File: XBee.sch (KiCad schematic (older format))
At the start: 3 parts, among them U2 XBEE

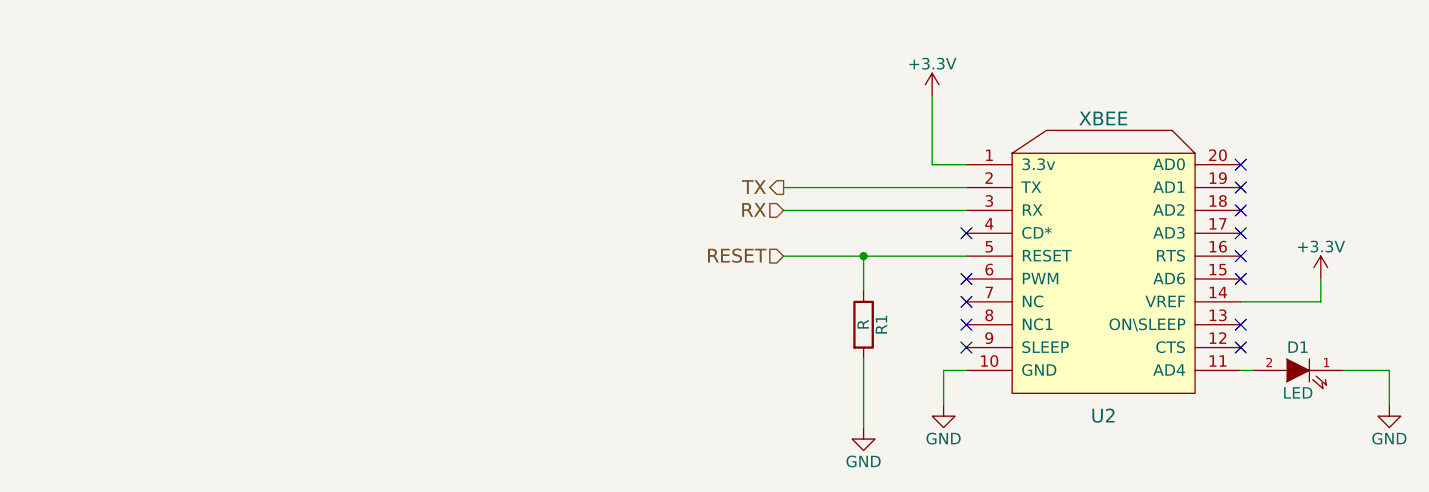
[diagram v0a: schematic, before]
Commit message: Placement in progress. XBee module 3d model
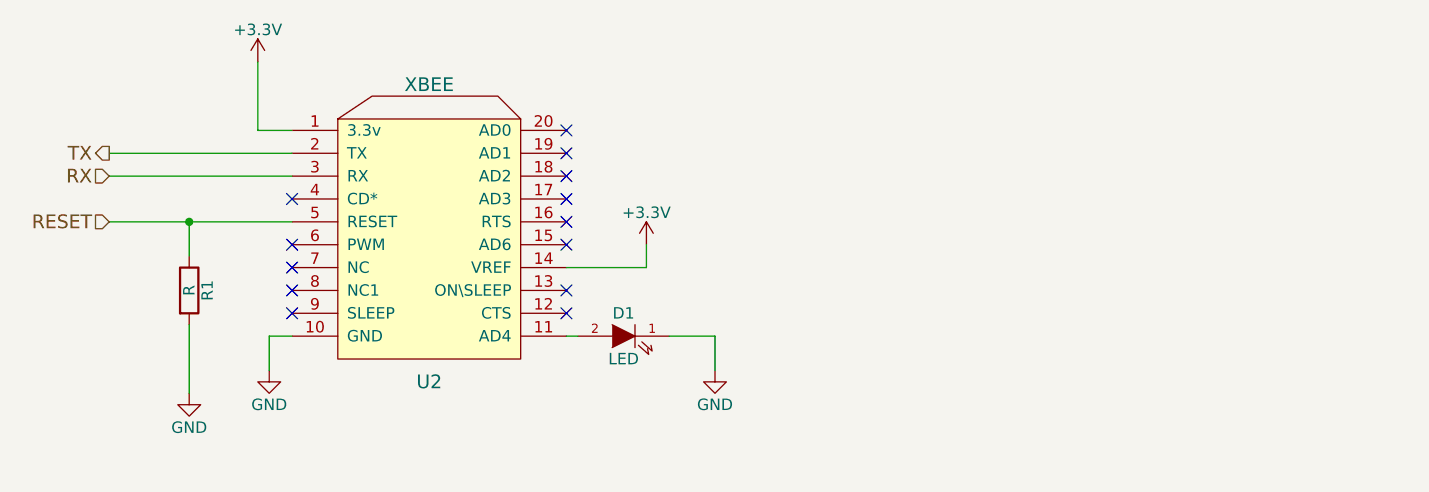
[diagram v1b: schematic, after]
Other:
- moved on the sheet: D1, R1, U2
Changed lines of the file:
@@
 Comment4 ""
 $EndDescr
-Text HLabel 5450 3200 0    60   Input ~ 0
+Text HLabel 2500 3050 0    60   Input ~ 0
 RESET
-Text HLabel 5450 2900 0    60   Output ~ 0
+Text HLabel 2500 2750 0    60   Output ~ 0
 TX
-Text HLabel 5450 3000 0    60   Input ~ 0
+Text HLabel 2500 2850 0    60   Input ~ 0
 RX
 Wire Wire Line
-	5450 2900 6250 2900
+	2500 2750 3300 2750
 Wire Wire Line
-	5450 3000 6250 3000
+	2500 2850 3300 2850
 Wire Wire Line
-	5450 3200 6250 3200
+	2500 3050 3300 3050
 $Comp
 L R R1
 U 1 1 583259C8
-P 5800 3500
-F 0 "R1" V 5880 3500 50  0000 C CNN
-F 1 "R" V 5800 3500 50  0000 C CNN
-F 2 "footprints:R_0603" V 5730 3500 50  0001 C CNN
-F 3 "" H 5800 3500 50  0000 C CNN
-	1    5800 3500
+P 2850 3350
+F 0 "R1" V 2930 3350 50  0000 C CNN
+F 1 "R" V 2850 3350 50  0000 C CNN
+F 2 "footprints:R_0603" V 2780 3350 50  0001 C CNN
+F 3 "" H 2850 3350 50  0000 C CNN
+	1    2850 3350
 	1    0    0    -1
 $EndComp
@@
 L LED D1
 U 1 1 583259E1
-P 7700 3700
-F 0 "D1" H 7700 3800 50  0000 C CNN
-F 1 "LED" H 7700 3600 50  0000 C CNN
-F 2 "footprints:LED-3MM" H 7700 3700 50  0001 C CNN
-F 3 "" H 7700 3700 50  0000 C CNN
-	1    7700 3700
+P 4750 3550
+F 0 "D1" H 4750 3650 50  0000 C CNN
+F 1 "LED" H 4750 3450 50  0000 C CNN
+F 2 "footprints:LED-3MM" H 4750 3550 50  0001 C CNN
+F 3 "" H 4750 3550 50  0000 C CNN
+	1    4750 3550
 	-1   0    0    -1
 $EndComp
@@
 L GND #PWR011
 U 1 1 583259FC
-P 8100 3850
-F 0 "#PWR011" H 8100 3600 50  0001 C CNN
-F 1 "GND" H 8100 3700 50  0000 C CNN
-F 2 "" H 8100 3850 50  0000 C CNN
-F 3 "" H 8100 3850 50  0000 C CNN
-	1    8100 3850
+P 5150 3700
+F 0 "#PWR011" H 5150 3450 50  0001 C CNN
+F 1 "GND" H 5150 3550 50  0000 C CNN
+F 2 "" H 5150 3700 50  0000 C CNN
+F 3 "" H 5150 3700 50  0000 C CNN
+	1    5150 3700
 	1    0    0    -1
 $EndComp
@@
 L GND #PWR012
 U 1 1 58325A17
-P 6150 3850
-F 0 "#PWR012" H 6150 3600 50  0001 C CNN
-F 1 "GND" H 6150 3700 50  0000 C CNN
-F 2 "" H 6150 3850 50  0000 C CNN
-F 3 "" H 6150 3850 50  0000 C CNN
-	1    6150 3850
+P 3200 3700
+F 0 "#PWR012" H 3200 3450 50  0001 C CNN
+F 1 "GND" H 3200 3550 50  0000 C CNN
+F 2 "" H 3200 3700 50  0000 C CNN
+F 3 "" H 3200 3700 50  0000 C CNN
+	1    3200 3700
 	1    0    0    -1
 $EndComp
@@
 L GND #PWR013
 U 1 1 58325A2B
-P 5800 3950
-F 0 "#PWR013" H 5800 3700 50  0001 C CNN
-F 1 "GND" H 5800 3800 50  0000 C CNN
-F 2 "" H 5800 3950 50  0000 C CNN
-F 3 "" H 5800 3950 50  0000 C CNN
-	1    5800 3950
+P 2850 3800
+F 0 "#PWR013" H 2850 3550 50  0001 C CNN
+F 1 "GND" H 2850 3650 50  0000 C CNN
+F 2 "" H 2850 3800 50  0000 C CNN
+F 3 "" H 2850 3800 50  0000 C CNN
+	1    2850 3800
 	1    0    0    -1
 $EndComp
@@
 L +3.3V #PWR014
 U 1 1 58325A3E
-P 6100 2500
-F 0 "#PWR014" H 6100 2350 50  0001 C CNN
-F 1 "+3.3V" H 6100 2640 50  0000 C CNN
-F 2 "" H 6100 2500 50  0000 C CNN
-F 3 "" H 6100 2500 50  0000 C CNN
-	1    6100 2500
+P 3150 2350
+F 0 "#PWR014" H 3150 2200 50  0001 C CNN
+F 1 "+3.3V" H 3150 2490 50  0000 C CNN
+F 2 "" H 3150 2350 50  0000 C CNN
+F 3 "" H 3150 2350 50  0000 C CNN
+	1    3150 2350
 	1    0    0    -1
 $EndComp
 Wire Wire Line
-	6100 2500 6100 2800
+	3150 2350 3150 2650
 Wire Wire Line
-	6100 2800 6250 2800
+	3150 2650 3300 2650
 Wire Wire Line
-	5800 3350 5800 3200
-Connection ~ 5800 3200
+	2850 3200 2850 3050
+Connection ~ 2850 3050
 Wire Wire Line
-	6250 3700 6150 3700
+	3300 3550 3200 3550
 Wire Wire Line
-	6150 3700 6150 3850
-NoConn ~ 6250 3100
-NoConn ~ 6250 3300
-NoConn ~ 6250 3400
-NoConn ~ 6250 3500
-NoConn ~ 6250 3600
-NoConn ~ 7450 3500
-NoConn ~ 7450 3600
-NoConn ~ 7450 2800
-NoConn ~ 7450 2900
-NoConn ~ 7450 3000
-NoConn ~ 7450 3100
-NoConn ~ 7450 3200
-NoConn ~ 7450 3300
+	3200 3550 3200 3700
+NoConn ~ 3300 2950
+NoConn ~ 3300 3150
+NoConn ~ 3300 3250
+NoConn ~ 3300 3350
+NoConn ~ 3300 3450
+NoConn ~ 4500 3350
+NoConn ~ 4500 3450
+NoConn ~ 4500 2650
+NoConn ~ 4500 2750
+NoConn ~ 4500 2850
+NoConn ~ 4500 2950
+NoConn ~ 4500 3050
+NoConn ~ 4500 3150
 $Comp
 L +3.3V #PWR015
 U 1 1 58325B5C
-P 7800 3300
-F 0 "#PWR015" H 7800 3150 50  0001 C CNN
-F 1 "+3.3V" H 7800 3440 50  0000 C CNN
-F 2 "" H 7800 3300 50  0000 C CNN
-F 3 "" H 7800 3300 50  0000 C CNN
-	1    7800 3300
+P 4850 3150
+F 0 "#PWR015" H 4850 3000 50  0001 C CNN
+F 1 "+3.3V" H 4850 3290 50  0000 C CNN
+F 2 "" H 4850 3150 50  0000 C CNN
+F 3 "" H 4850 3150 50  0000 C CNN
+	1    4850 3150
 	1    0    0    -1
 $EndComp
 Wire Wire Line
-	7800 3300 7800 3400
+	4850 3150 4850 3250
 Wire Wire Line
-	7800 3400 7450 3400
+	4850 3250 4500 3250
 Wire Wire Line
-	7500 3700 7450 3700
+	4550 3550 4500 3550
 Wire Wire Line
-	7900 3700 8100 3700
+	4950 3550 5150 3550
 Wire Wire Line
-	8100 3700 8100 3850
+	5150 3550 5150 3700
 Wire Wire Line
-	5800 3650 5800 3950
+	2850 3500 2850 3800
 $Comp
 L XBEE U2
 U 1 1 58325202
-P 6850 3350
-F 0 "U2" H 6850 2800 60  0000 C CNN
-F 1 "XBEE" H 6850 4100 60  0000 C CNN
-F 2 "XBee:XBee-pro" H 6850 3350 60  0001 C CNN
-F 3 "" H 6850 3350 60  0000 C CNN
-	1    6850 3350
+P 3900 3200
+F 0 "U2" H 3900 2650 60  0000 C CNN
+F 1 "XBEE" H 3900 3950 60  0000 C CNN
+F 2 "XBee:XBee-pro" H 3900 3200 60  0001 C CNN
+F 3 "" H 3900 3200 60  0000 C CNN
+	1    3900 3200
 	1    0    0    -1
 $EndComp

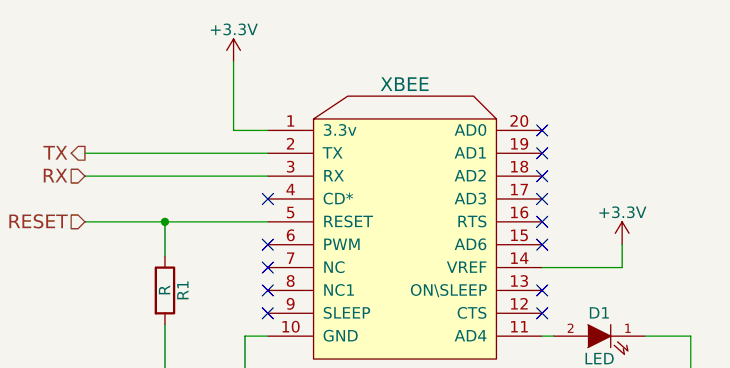
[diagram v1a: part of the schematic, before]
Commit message: Corregido: footprint batería, footprint GY-521, conector poncho para pasar ERC en esquemático, placement de footprints, dimensión del poncho para dejar descubierto el botón de reset de la EDU-CIAA. Agregado: agujeros de sujeción en la parte superior del poncho.
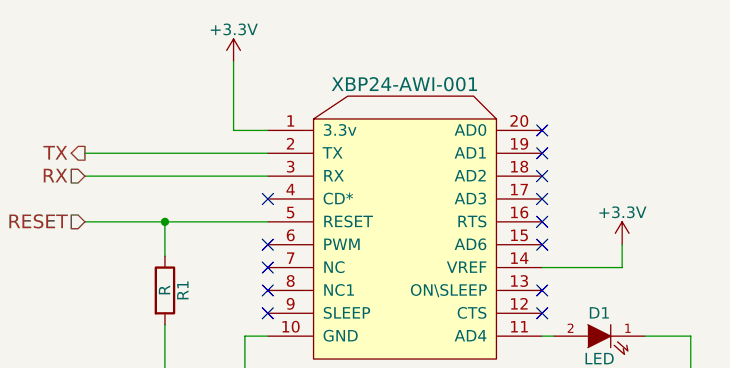
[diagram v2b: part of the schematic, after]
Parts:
- U2: value XBEE -> XBP24-AWI-001; Manf (none) -> DIGI
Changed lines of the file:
@@
 $EndComp
 $Comp
-L GND #PWR011
+L GND #PWR013
 U 1 1 583259FC
 P 5150 3700
-F 0 "#PWR011" H 5150 3450 50  0001 C CNN
+F 0 "#PWR013" H 5150 3450 50  0001 C CNN
 F 1 "GND" H 5150 3550 50  0000 C CNN
 F 2 "" H 5150 3700 50  0000 C CNN
@@
 $EndComp
 $Comp
-L GND #PWR012
+L GND #PWR014
 U 1 1 58325A17
 P 3200 3700
-F 0 "#PWR012" H 3200 3450 50  0001 C CNN
+F 0 "#PWR014" H 3200 3450 50  0001 C CNN
 F 1 "GND" H 3200 3550 50  0000 C CNN
 F 2 "" H 3200 3700 50  0000 C CNN
@@
 $EndComp
 $Comp
-L GND #PWR013
+L GND #PWR015
 U 1 1 58325A2B
 P 2850 3800
-F 0 "#PWR013" H 2850 3550 50  0001 C CNN
+F 0 "#PWR015" H 2850 3550 50  0001 C CNN
 F 1 "GND" H 2850 3650 50  0000 C CNN
 F 2 "" H 2850 3800 50  0000 C CNN
@@
 $EndComp
 $Comp
-L +3.3V #PWR014
+L +3.3V #PWR016
 U 1 1 58325A3E
 P 3150 2350
-F 0 "#PWR014" H 3150 2200 50  0001 C CNN
+F 0 "#PWR016" H 3150 2200 50  0001 C CNN
 F 1 "+3.3V" H 3150 2490 50  0000 C CNN
 F 2 "" H 3150 2350 50  0000 C CNN
@@
 NoConn ~ 4500 3150
 $Comp
-L +3.3V #PWR015
+L +3.3V #PWR017
 U 1 1 58325B5C
 P 4850 3150
-F 0 "#PWR015" H 4850 3000 50  0001 C CNN
+F 0 "#PWR017" H 4850 3000 50  0001 C CNN
 F 1 "+3.3V" H 4850 3290 50  0000 C CNN
 F 2 "" H 4850 3150 50  0000 C CNN
@@
 P 3900 3200
 F 0 "U2" H 3900 2650 60  0000 C CNN
-F 1 "XBEE" H 3900 3950 60  0000 C CNN
+F 1 "XBP24-AWI-001" H 3900 3950 60  0000 C CNN
 F 2 "XBee:XBee-pro" H 3900 3200 60  0001 C CNN
-F 3 "" H 3900 3200 60  0000 C CNN
+F 3 "https://www.digi.com/pdf/ds_xbeemultipointmodules.pdf" H 3900 3200 60  0001 C CNN
+F 4 "DIGI" H 3900 3200 60  0001 C CNN "Manf"
+F 5 "XB24-AWI-001
+" H 3900 3200 60  0001 C CNN "Manf#"
+F 6 "XB24-AWI-001-ND
+" H 3900 3200 60  0001 C CNN "Digikey#"
+F 7 "888-XB24-AWI-001
+" H 3900 3200 60  0001 C CNN "Mouser#"
 	1    3900 3200
 	1    0    0    -1

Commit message: Ruteo. Correciones. Cambio de footprint del switch.
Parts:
- U2: value XBP24-AWI-001 -> XBEE; footprint XBee:XBee-pro -> footprints:XBee-pro; Desc (none) -> XBee-PRO S1 802.15.4 extended-range module w/ wire antenna; Manf# (none) -> XBP24-AWI-001
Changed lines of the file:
@@
 encoding utf-8
 Sheet 3 4
-Title ""
-Date ""
-Rev ""
+Title "Poncho Misión SAEv2 - Módulo XBee"
+Date "2016-12-14"
+Rev "1.0"
 Comp ""
-Comment1 ""
-Comment2 ""
+Comment1 "Autores: Julián Iglesias / Elli Carlos"
+Comment2 "Licencia: BSD"
 Comment3 ""
 Comment4 ""
@@
 $Comp
 L XBEE U2
-U 1 1 58325202
+U 1 1 5851DFE8
 P 3900 3200
 F 0 "U2" H 3900 2650 60  0000 C CNN
-F 1 "XBP24-AWI-001" H 3900 3950 60  0000 C CNN
-F 2 "XBee:XBee-pro" H 3900 3200 60  0001 C CNN
+F 1 "XBEE" H 3900 3950 60  0000 C CNN
+F 2 "footprints:XBee-pro" H 3900 3200 60  0001 C CNN
 F 3 "https://www.digi.com/pdf/ds_xbeemultipointmodules.pdf" H 3900 3200 60  0001 C CNN
-F 4 "DIGI" H 3900 3200 60  0001 C CNN "Manf"
-F 5 "XB24-AWI-001
-" H 3900 3200 60  0001 C CNN "Manf#"
-F 6 "XB24-AWI-001-ND
+F 4 "XBee-PRO S1 802.15.4 extended-range module w/ wire antenna" H 3900 3200 60  0001 C CNN "Desc"
+F 5 "DIGI" H 3900 3200 60  0001 C CNN "Manf"
+F 6 "XBP24-AWI-001" H 3900 3200 60  0001 C CNN "Manf#"
+F 7 "XBP24-AWI-001-ND
 " H 3900 3200 60  0001 C CNN "Digikey#"
-F 7 "888-XB24-AWI-001
+F 8 "888-XBP24-AWI-001
 " H 3900 3200 60  0001 C CNN "Mouser#"
 	1    3900 3200

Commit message: Corrección de errores in progress...
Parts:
- U2: Desc XBee-PRO S1 802.15.4 extended-range module w/ wire antenna -> XBee Pro Series1 Wire antenna; Digikey# (none) -> XBP24-AWI-001-ND; Mouser# (none) -> 888-XBP24-AWI-001
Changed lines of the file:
@@
 EESchema Schematic File Version 2
-LIBS:Mision_SAE-rescue
 LIBS:power
-LIBS:device
-LIBS:conn
-LIBS:mpu-6050
-LIBS:power1
-LIBS:xbee
-LIBS:basico
-LIBS:GY-65
-LIBS:GY-521
 LIBS:Mision_SAE-cache
 EELAYER 25 0
@@
 encoding utf-8
 Sheet 3 4
-Title "Poncho Misión SAEv2 - Módulo XBee"
-Date "2016-12-14"
+Title "Poncho Misión SAEv2 - Esquemático jerárquico"
+Date "2016-12-21"
 Rev "1.0"
 Comp ""
-Comment1 "Autores: Julián Iglesias / Elli Carlos"
-Comment2 "Licencia: BSD"
-Comment3 ""
+Comment1 "Autores: Julián Iglesias / Elli Carlos."
+Comment2 "Revisor: Matías Marando"
+Comment3 "Licencia: BSD"
 Comment4 ""
 $EndDescr
@@
 $EndComp
 $Comp
-L GND #PWR013
+L GND #PWR011
 U 1 1 583259FC
 P 5150 3700
-F 0 "#PWR013" H 5150 3450 50  0001 C CNN
+F 0 "#PWR011" H 5150 3450 50  0001 C CNN
 F 1 "GND" H 5150 3550 50  0000 C CNN
 F 2 "" H 5150 3700 50  0000 C CNN
@@
 $EndComp
 $Comp
-L GND #PWR014
+L GND #PWR012
 U 1 1 58325A17
 P 3200 3700
-F 0 "#PWR014" H 3200 3450 50  0001 C CNN
+F 0 "#PWR012" H 3200 3450 50  0001 C CNN
 F 1 "GND" H 3200 3550 50  0000 C CNN
 F 2 "" H 3200 3700 50  0000 C CNN
@@
 $EndComp
 $Comp
-L GND #PWR015
+L GND #PWR013
 U 1 1 58325A2B
 P 2850 3800
-F 0 "#PWR015" H 2850 3550 50  0001 C CNN
+F 0 "#PWR013" H 2850 3550 50  0001 C CNN
 F 1 "GND" H 2850 3650 50  0000 C CNN
 F 2 "" H 2850 3800 50  0000 C CNN
@@
 $EndComp
 $Comp
-L +3.3V #PWR016
+L +3.3V #PWR014
 U 1 1 58325A3E
 P 3150 2350
-F 0 "#PWR016" H 3150 2200 50  0001 C CNN
+F 0 "#PWR014" H 3150 2200 50  0001 C CNN
 F 1 "+3.3V" H 3150 2490 50  0000 C CNN
 F 2 "" H 3150 2350 50  0000 C CNN
@@
 NoConn ~ 4500 3150
 $Comp
-L +3.3V #PWR017
+L +3.3V #PWR015
 U 1 1 58325B5C
 P 4850 3150
-F 0 "#PWR017" H 4850 3000 50  0001 C CNN
+F 0 "#PWR015" H 4850 3000 50  0001 C CNN
 F 1 "+3.3V" H 4850 3290 50  0000 C CNN
 F 2 "" H 4850 3150 50  0000 C CNN
@@
 $Comp
 L XBEE U2
-U 1 1 5851DFE8
+U 1 1 585B02E9
 P 3900 3200
 F 0 "U2" H 3900 2650 60  0000 C CNN
@@
 F 2 "footprints:XBee-pro" H 3900 3200 60  0001 C CNN
 F 3 "https://www.digi.com/pdf/ds_xbeemultipointmodules.pdf" H 3900 3200 60  0001 C CNN
-F 4 "XBee-PRO S1 802.15.4 extended-range module w/ wire antenna" H 3900 3200 60  0001 C CNN "Desc"
+F 4 "XBee Pro Series1 Wire antenna" H 3900 3200 60  0001 C CNN "Desc"
 F 5 "DIGI" H 3900 3200 60  0001 C CNN "Manf"
 F 6 "XBP24-AWI-001" H 3900 3200 60  0001 C CNN "Manf#"
-F 7 "XBP24-AWI-001-ND
-" H 3900 3200 60  0001 C CNN "Digikey#"
-F 8 "888-XBP24-AWI-001
-" H 3900 3200 60  0001 C CNN "Mouser#"
+F 7 "XBP24-AWI-001-ND" H 3900 3200 60  0001 C CNN "Digikey#"
+F 8 "888-XBP24-AWI-001" H 3900 3200 60  0001 C CNN "Mouser#"
 	1    3900 3200
 	1    0    0    -1
